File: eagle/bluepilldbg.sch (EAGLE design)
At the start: 10 parts

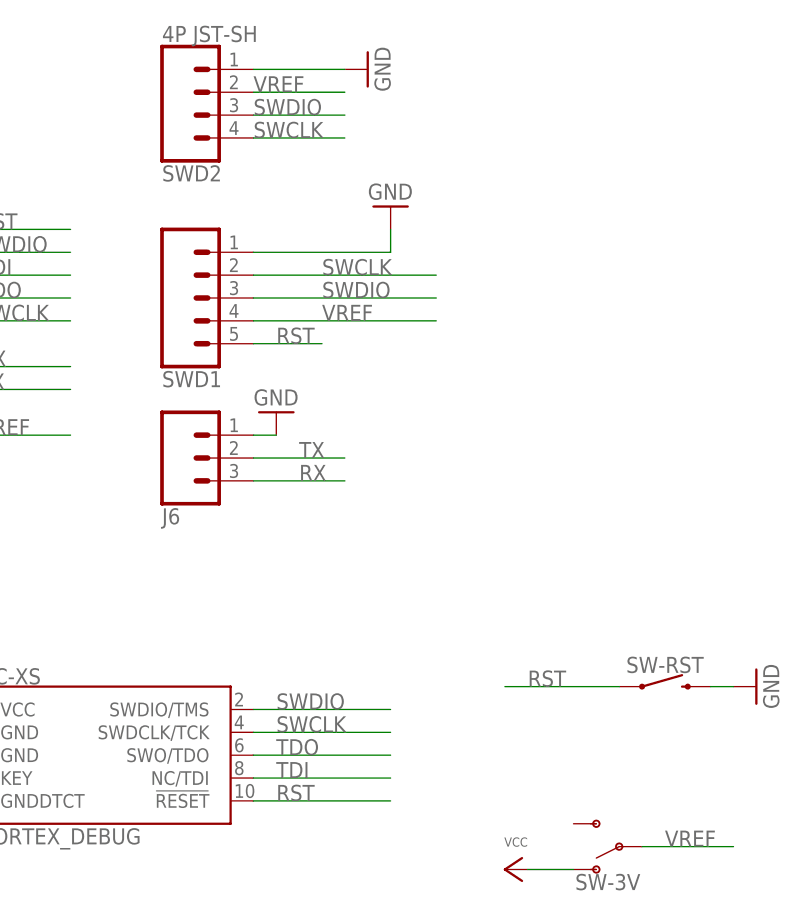
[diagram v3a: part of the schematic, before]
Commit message: add part numbers and BOM
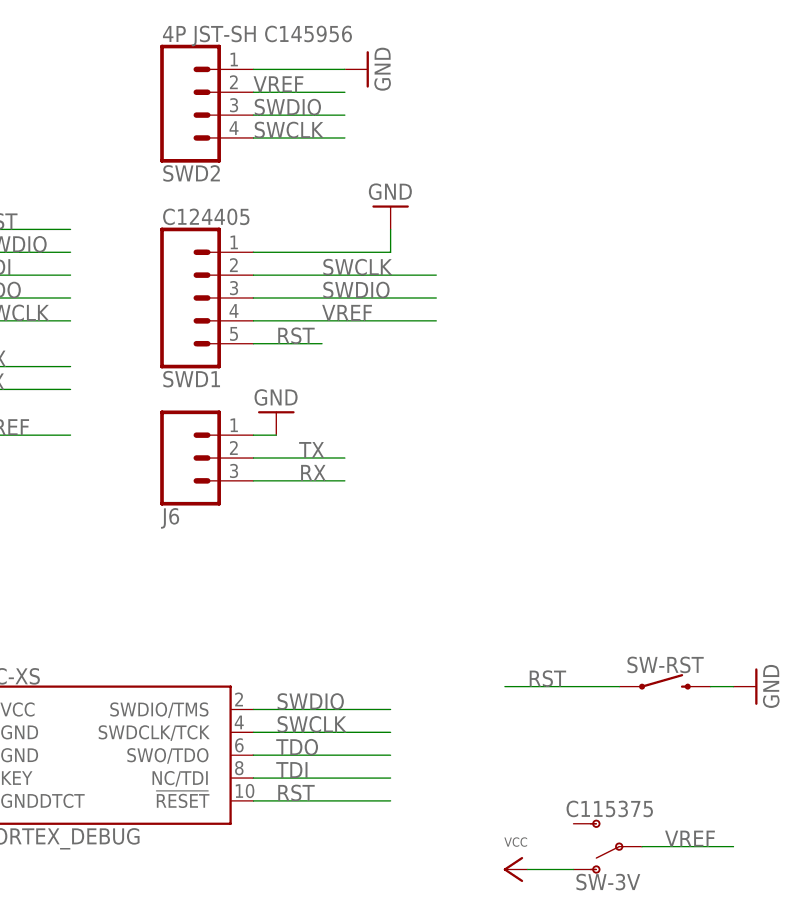
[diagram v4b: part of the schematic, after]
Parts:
- SW-3V: value (none) -> C115375
- SW-RST: value MOMENTARY-SWITCH-SPST-SMD-6.0X3.5MM -> C255816
- SWD1: value (none) -> C124405
- SWD2: value 4P JST-SH -> 4P JST-SH C145956
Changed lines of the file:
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@@
 <grid distance="0.1" unitdist="inch" unit="inch" style="lines" multiple="1" display="no" altdistance="0.01" altunitdist="inch" altunit="inch"/>
 <layers>
-<layer number="1" name="Top" color="4" fill="1" visible="yes" active="no"/>
-<layer number="16" name="Bottom" color="1" fill="1" visible="yes" active="no"/>
-<layer number="17" name="Pads" color="2" fill="1" visible="yes" active="no"/>
-<layer number="18" name="Vias" color="2" fill="1" visible="yes" active="no"/>
-<layer number="19" name="Unrouted" color="6" fill="1" visible="yes" active="no"/>
-<layer number="20" name="Dimension" color="30" fill="1" visible="yes" active="no"/>
-<layer number="21" name="tPlace" color="16" fill="1" visible="yes" active="no"/>
-<layer number="22" name="bPlace" color="24" fill="1" visible="yes" active="no"/>
-<layer number="23" name="tOrigins" color="15" fill="1" visible="yes" active="no"/>
-<layer number="24" name="bOrigins" color="15" fill="1" visible="yes" active="no"/>
-<layer number="25" name="tNames" color="25" fill="1" visible="yes" active="no"/>
-<layer number="26" name="bNames" color="25" fill="1" visible="yes" active="no"/>
-<layer number="27" name="tValues" color="7" fill="1" visible="yes" active="no"/>
-<layer number="28" name="bValues" color="7" fill="1" visible="yes" active="no"/>
+<layer number="1" name="Top" color="4" fill="1" visible="no" active="no"/>
+<layer number="16" name="Bottom" color="1" fill="1" visible="no" active="no"/>
+<layer number="17" name="Pads" color="2" fill="1" visible="no" active="no"/>
+<layer number="18" name="Vias" color="2" fill="1" visible="no" active="no"/>
+<layer number="19" name="Unrouted" color="6" fill="1" visible="no" active="no"/>
+<layer number="20" name="Dimension" color="30" fill="1" visible="no" active="no"/>
+<layer number="21" name="tPlace" color="16" fill="1" visible="no" active="no"/>
+<layer number="22" name="bPlace" color="24" fill="1" visible="no" active="no"/>
+<layer number="23" name="tOrigins" color="15" fill="1" visible="no" active="no"/>
+<layer number="24" name="bOrigins" color="15" fill="1" visible="no" active="no"/>
+<layer number="25" name="tNames" color="25" fill="1" visible="no" active="no"/>
+<layer number="26" name="bNames" color="25" fill="1" visible="no" active="no"/>
+<layer number="27" name="tValues" color="7" fill="1" visible="no" active="no"/>
+<layer number="28" name="bValues" color="7" fill="1" visible="no" active="no"/>
 <layer number="29" name="tStop" color="7" fill="3" visible="no" active="no"/>
 <layer number="30" name="bStop" color="7" fill="6" visible="no" active="no"/>
@@
 <layer number="35" name="tGlue" color="7" fill="4" visible="no" active="no"/>
 <layer number="36" name="bGlue" color="7" fill="5" visible="no" active="no"/>
-<layer number="37" name="tTest" color="7" fill="1" visible="yes" active="no"/>
-<layer number="38" name="bTest" color="7" fill="1" visible="yes" active="no"/>
+<layer number="37" name="tTest" color="7" fill="1" visible="no" active="no"/>
+<layer number="38" name="bTest" color="7" fill="1" visible="no" active="no"/>
 <layer number="39" name="tKeepout" color="4" fill="11" visible="no" active="no"/>
 <layer number="40" name="bKeepout" color="1" fill="11" visible="no" active="no"/>
@@
 <layer number="44" name="Drills" color="7" fill="1" visible="no" active="no"/>
 <layer number="45" name="Holes" color="7" fill="1" visible="no" active="no"/>
-<layer number="46" name="Milling" color="3" fill="1" visible="yes" active="no"/>
-<layer number="47" name="Measures" color="7" fill="1" visible="yes" active="no"/>
-<layer number="48" name="Document" color="7" fill="1" visible="yes" active="no"/>
-<layer number="49" name="Reference" color="7" fill="1" visible="yes" active="no"/>
-<layer number="50" name="dxf" color="7" fill="1" visible="yes" active="no"/>
-<layer number="51" name="tDocu" color="6" fill="1" visible="yes" active="no"/>
-<layer number="52" name="bDocu" color="7" fill="1" visible="yes" active="no"/>
-<layer number="53" name="tGND_GNDA" color="7" fill="9" visible="yes" active="no"/>
-<layer number="54" name="bGND_GNDA" color="1" fill="9" visible="yes" active="no"/>
-<layer number="56" name="wert" color="7" fill="1" visible="yes" active="no"/>
-<layer number="57" name="tCAD" color="7" fill="1" visible="yes" active="no"/>
-<layer number="58" name="bCAD" color="11" fill="1" visible="yes" active="no"/>
-<layer number="59" name="tCarbon" color="7" fill="1" visible="yes" active="no"/>
-<layer number="60" name="bCarbon" color="7" fill="1" visible="yes" active="no"/>
-<layer number="61" name="stand" color="7" fill="1" visible="yes" active="no"/>
+<layer number="46" name="Milling" color="3" fill="1" visible="no" active="no"/>
+<layer number="47" name="Measures" color="7" fill="1" visible="no" active="no"/>
+<layer number="48" name="Document" color="7" fill="1" visible="no" active="no"/>
+<layer number="49" name="Reference" color="7" fill="1" visible="no" active="no"/>
+<layer number="50" name="dxf" color="7" fill="1" visible="no" active="no"/>
+<layer number="51" name="tDocu" color="6" fill="1" visible="no" active="no"/>
+<layer number="52" name="bDocu" color="7" fill="1" visible="no" active="no"/>
+<layer number="53" name="tGND_GNDA" color="7" fill="9" visible="no" active="no"/>
+<layer number="54" name="bGND_GNDA" color="1" fill="9" visible="no" active="no"/>
+<layer number="56" name="wert" color="7" fill="1" visible="no" active="no"/>
+<layer number="57" name="tCAD" color="7" fill="1" visible="no" active="no"/>
+<layer number="58" name="bCAD" color="11" fill="1" visible="no" active="no"/>
+<layer number="59" name="tCarbon" color="7" fill="1" visible="no" active="no"/>
+<layer number="60" name="bCarbon" color="7" fill="1" visible="no" active="no"/>
+<layer number="61" name="stand" color="7" fill="1" visible="no" active="no"/>
 <layer number="88" name="SimResults" color="9" fill="1" visible="yes" active="yes"/>
 <layer number="89" name="SimProbes" color="9" fill="1" visible="yes" active="yes"/>
@@
 <part name="GND2" library="BrainPad MAX" deviceset="GND" device=""/>
 <part name="GND3" library="BrainPad MAX" deviceset="GND" device=""/>
-<part name="SW-3V" library="pcnt" deviceset="SWITCH-SPDT" device="-SMD-AYZ0202"/>
-<part name="SW-RST" library="mb-arcade-shield" deviceset="MOMENTARY-SWITCH-SPST" device="-SMD-6.0X3.5MM"/>
+<part name="SW-3V" library="pcnt" deviceset="SWITCH-SPDT" device="-SMD-AYZ0202" value="C115375"/>
+<part name="SW-RST" library="mb-arcade-shield" deviceset="MOMENTARY-SWITCH-SPST" device="-SMD-6.0X3.5MM" value="C255816"/>
 <part name="P+2" library="mb-arcade-shield" deviceset="VCC" device=""/>
 <part name="GND6" library="BrainPad MAX" deviceset="GND" device=""/>
 <part name="J6" library="pcnt" deviceset="CONN_03" device="1X03_NO_SILK"/>
 <part name="GND7" library="BrainPad MAX" deviceset="GND" device=""/>
-<part name="SWD1" library="pcnt" deviceset="CONN_05" device="SMALLHOLE"/>
+<part name="SWD1" library="pcnt" deviceset="CONN_05" device="SMALLHOLE" value="C124405"/>
 <part name="JMP1" library="pcnt" deviceset="SWITCH-SPDT" device="-HD"/>
-<part name="SWD2" library="pcnt" deviceset="CONN_04" device="SMD2" value="4P JST-SH">
+<part name="SWD2" library="pcnt" deviceset="CONN_04" device="SMD2" value="4P JST-SH C145956">
 <attribute name="SPICEPREFIX" value="S"/>
 </part>
